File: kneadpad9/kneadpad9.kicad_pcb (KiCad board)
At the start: 2 copper layers, 90.5 x 57.1 mm, 11 parts, among them SW1 SW_Push, SW2 SW_Push, SW3 SW_Push, SW4 SW_Push, SW5 SW_Push, SW6 SW_Push, SW7 SW_Push, SW8 SW_Push, SW9 SW_Push, U1 Pico

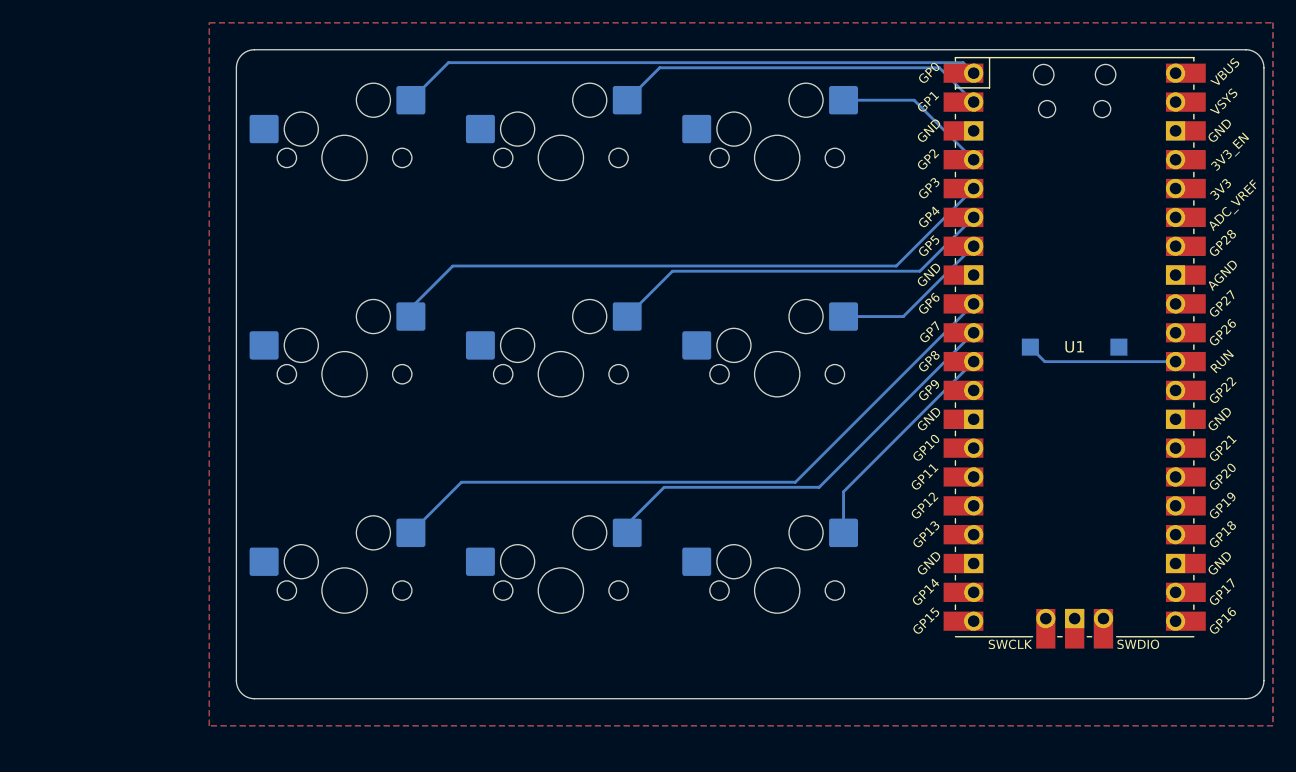
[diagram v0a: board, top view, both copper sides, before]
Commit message: Add M2 mounting holes for backplate
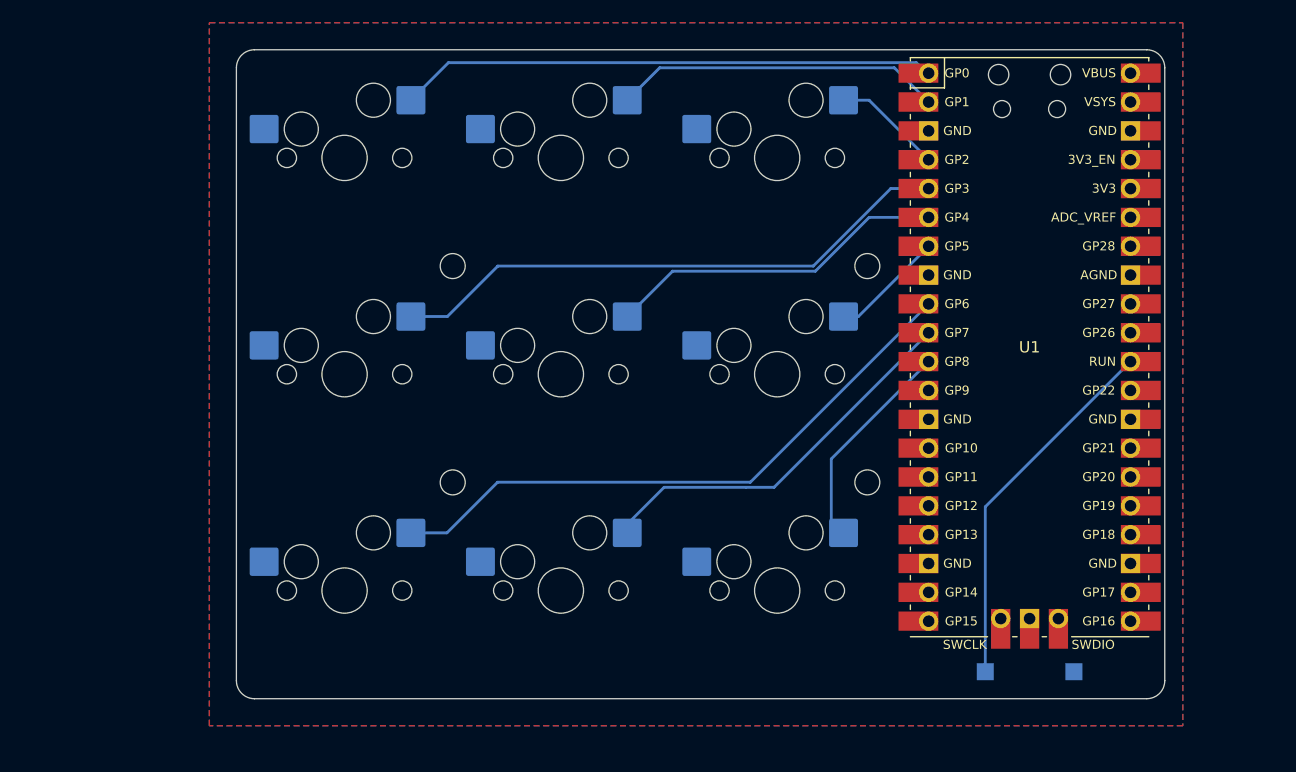
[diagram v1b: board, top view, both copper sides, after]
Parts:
- added REF**: MountingHole_2.2mm_M2, MountingHole:MountingHole_2.2mm_M2, F.Cu at (172.2, 77.0)
- added REF**: MountingHole_2.2mm_M2, MountingHole:MountingHole_2.2mm_M2, F.Cu at (135.7, 77.0)
- added REF**: MountingHole_2.2mm_M2, MountingHole:MountingHole_2.2mm_M2, F.Cu at (172.2, 96.0)
- added REF**: MountingHole_2.2mm_M2, MountingHole:MountingHole_2.2mm_M2, F.Cu at (135.7, 96.0)
- moved RESET 28.8 mm to (186.5, 112.7)
- moved U1 3.97 mm to (186.5, 84.1)
- renumbered RESET1 to RESET
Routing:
- net reset: track 13.3 -> 32.6 mm
- net sw3: track 54.7 -> 50.3 mm
- net sw4: track 34.1 -> 30.2 mm
- net sw7: track 38.3 -> 34.3 mm
- net sw5: track 14.0 -> 10.1 mm
- net sw2: track 13.6 -> 9.66 mm
- net sw1: track 32.9 -> 29.0 mm
- net sw0: track 51.3 -> 47.3 mm
- net sw6: track 57.9 -> 53.9 mm
- net sw8: track 19.8 -> 19.1 mm
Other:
- board size 90.5 x 57.1 mm -> 81.8 x 57.1 mm

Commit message: Update edge cuts for better alignment
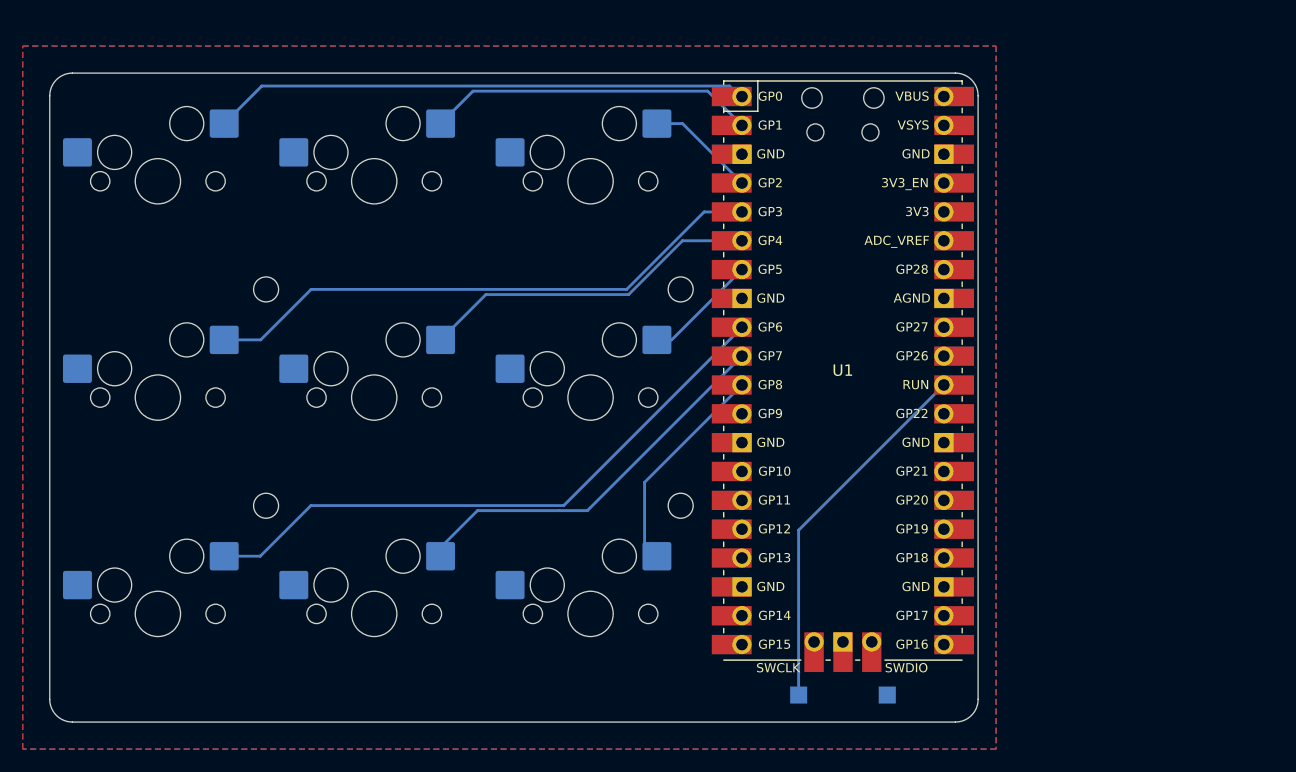
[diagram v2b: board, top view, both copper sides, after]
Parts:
- moved SW1 16.6 mm to (109.8, 69.5)
- moved SW2 16.6 mm to (128.8, 69.5)
- moved SW3 16.6 mm to (147.9, 69.5)
- moved SW4 16.6 mm to (109.8, 88.6)
- moved SW5 16.6 mm to (128.8, 88.6)
- moved SW6 16.6 mm to (147.9, 88.6)
- moved SW7 16.6 mm to (109.8, 107.6)
- moved SW8 16.6 mm to (128.8, 107.6)
- moved SW9 16.6 mm to (147.9, 107.6)
- moved REF** 16.6 mm to (155.8, 79.0)
- moved REF** 16.6 mm to (155.8, 98.1)
- moved RESET 16.6 mm to (170.1, 114.8)
- moved U1 16.6 mm to (170.1, 86.2)
- moved REF** 16.6 mm to (119.3, 79.0)
- moved REF** 16.6 mm to (119.3, 98.1)
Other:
- board size 81.8 x 57.1 mm -> 81.8 x 57.2 mm

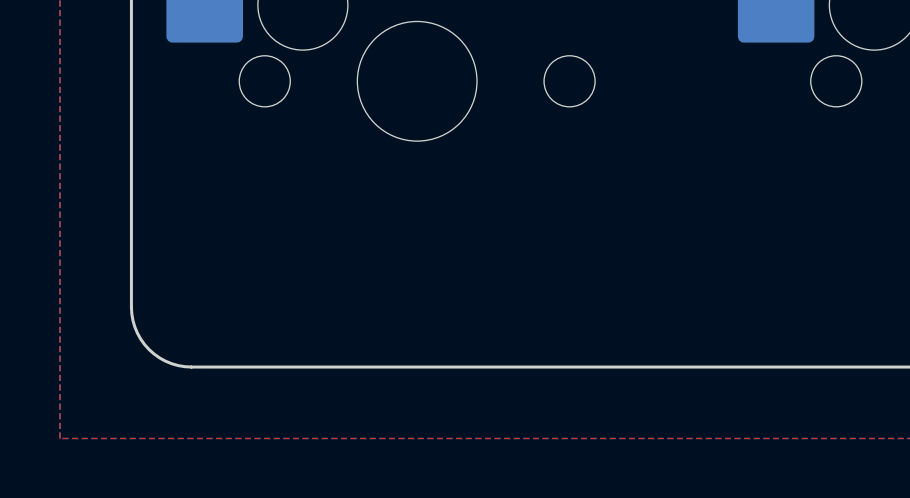
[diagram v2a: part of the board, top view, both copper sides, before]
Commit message: Added bottom and top plates, added silkscreen label
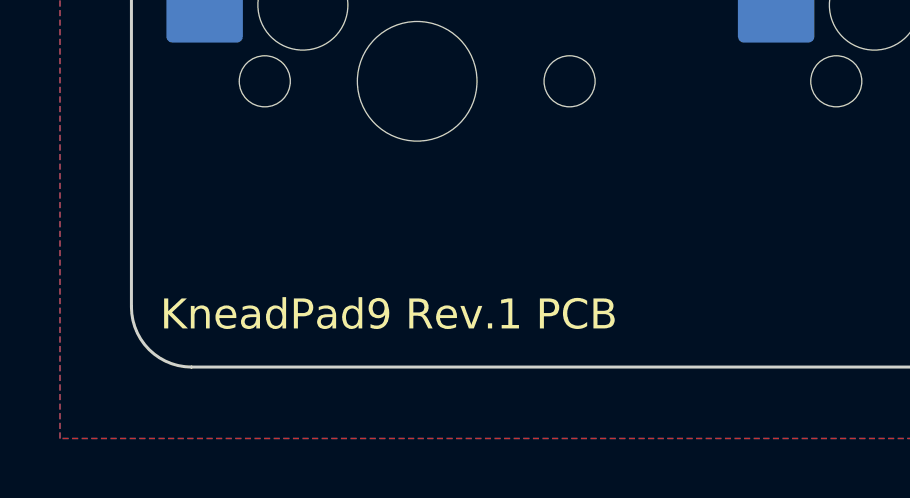
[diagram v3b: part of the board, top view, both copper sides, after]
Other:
- board text added: "KneadPad9 Rev.1 PCB"
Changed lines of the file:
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@@
   (gr_arc (start 100.24375 62) (mid 100.829536 60.585786) (end 102.24375 60) (layer "Edge.Cuts") (width 0.1))
   (gr_line (start 102.24375 117.15) (end 180 117.15) (layer "Edge.Cuts") (width 0.1))
+  (gr_text "KneadPad9 Rev.1 PCB" (at 101.2 115.4) (layer "F.SilkS")
+    (effects (font (size 1 1) (thickness 0.125)) (justify left))
+  )
   (segment (start 166.19375 114.76875) (end 166.19375 100.25375) (width 0.25) (layer "B.Cu") (net 2))
   (segment (start 166.19375 100.25375) (end 178.98375 87.46375) (width 0.25) (layer "B.Cu") (net 2))
